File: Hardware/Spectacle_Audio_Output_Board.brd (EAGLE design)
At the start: 25.4 x 55.9 mm, 86 parts, among them J4 AUDIO-JACK3, J5 AUDIO-JACK3, U1 CY8C4146LQI-S422, U2 3.3V, U3 3.3V, U4 AT25SF041-SOIC8, U5 VS1000, Y1 12MHz

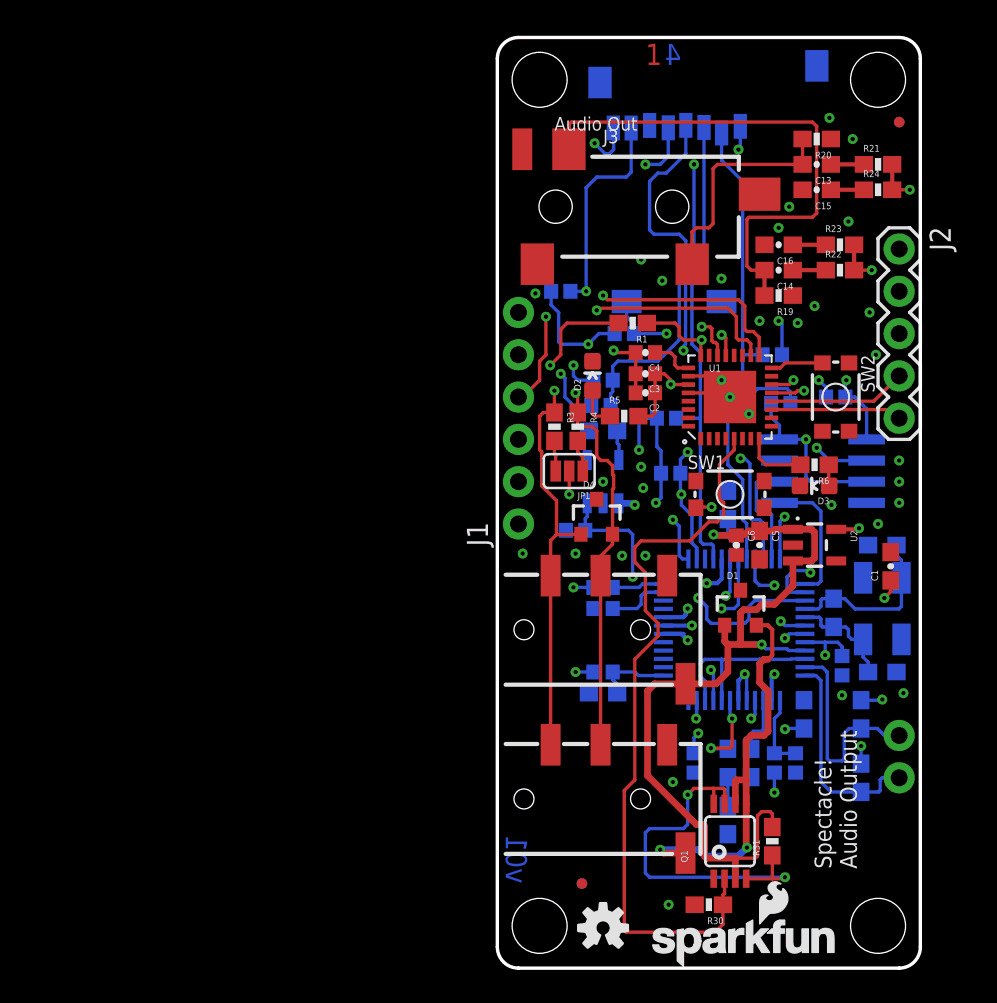
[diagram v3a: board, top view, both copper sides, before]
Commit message: Change pullup resistor values to 4.7k Add firmware to repo
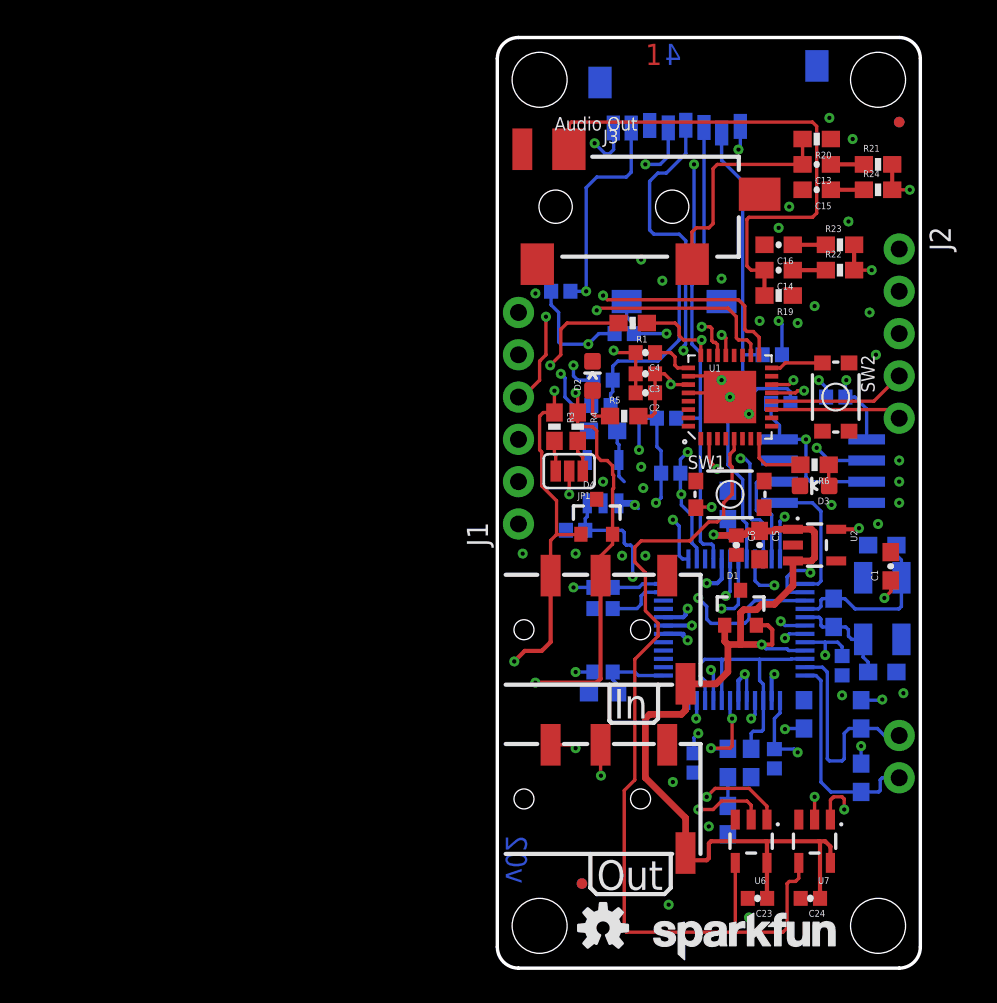
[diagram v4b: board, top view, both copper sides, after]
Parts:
- removed C21: 1.0uF, SparkFun-Capacitors:0402-CAP
- removed Q1: (no value), SparkFun-DiscreteSemi:MSOP8
- removed R30, R31: 10K, SparkFun-Resistors:0603-RES
- added C23, C24: 0.1uF, SparkFun-Capacitors:0402-CAP
- added U6, U7: SN74LVC1G66, SparkFun-AnalogIC:SOT23-5
- J2: device SparkFun-Connectors:1X05 -> SparkFun-Connectors:1X05_NO_SILK
- LOGO2: value SFE_LOGO_NAME_FLAME.1_INCH -> SFE_LOGO_NAME.1_INCH; device SparkFun-Aesthetics:SFE_LOGO_NAME_FLAME_.1 -> SparkFun-Aesthetics:SFE_LOGO_NAME_.1
- R3, R4: value 2.2k -> 4.7K
- moved R26 1.30 mm to (16.6, 12.6)
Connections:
- removed net N$15: C21.1, R26.1, U5.37
- removed net N$26: Q1.4, Q1.7, Q1.8, R31.1
- removed net VOUT: D1.2, J5.EARTH, Q1.5, Q1.6
- removed net V_OUT_EN: Q1.2, R30.1, U1.5
- new net I2C_OUT_EN: U1.5, U6.4, U7.4
- new net POWBTN: R26.1, U1.2, U5.37
- new net SCL_OUT: J5.RING2, U6.2
- new net SDA_OUT: J5.RING1, U7.2
- net 3.3V: no longer C21.2
- net GND: now also C23.2, C24.2, U6.3, U7.3; no longer Q1.1, R30.2
- net SCL: now also U6.1; no longer J5.RING2
- net SDA: now also U7.1; no longer J5.RING1
- net VIN: now also C23.1, C24.1, D1.2, J5.EARTH, U6.5, U7.5; no longer Q1.3, R31.2
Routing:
- net I2C_OUT_EN: track 0.00 -> 54.1 mm
- net V_OUT_EN: track 44.6 -> 0.00 mm
- net SDA: track 40.5 -> 72.9 mm, vias 2 -> 4
- net POWBTN: track 0.00 -> 28.3 mm, vias 0 -> 2
- net VOUT: track 25.1 -> 0.00 mm, vias 2 -> 0
- net N$26: track 23.4 -> 0.00 mm, vias 2 -> 0
- net SCL: track 44.2 -> 65.9 mm, vias 2 -> 4
- net SCL_OUT: track 0.00 -> 19.7 mm, vias 0 -> 2
- net SDA_OUT: track 0.00 -> 17.1 mm, vias 0 -> 2
- net VIN: track 57.1 -> 69.0 mm
- net N$15: track 4.58 -> 0.00 mm
- net VDD: track 26.6 -> 28.0 mm
- net 3.3V: track 31.0 -> 29.8 mm, vias 9 -> 8
- net GND: vias 38 -> 40
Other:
- board text added: "In"
- board text added: "Out"
- board text added: "v02"
- board text removed: "Spectacle\! Audio Output"
- board text removed: "v01"

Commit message: Changes from review/checklist
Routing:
- net VDD: track 28.0 -> 26.6 mm
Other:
- board text added: "Audio Output"
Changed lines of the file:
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@@
 <layers>
 <layer number="1" name="Top" color="4" fill="1" visible="yes" active="yes"/>
-<layer number="2" name="Route2" color="1" fill="3" visible="no" active="yes"/>
-<layer number="15" name="Route15" color="4" fill="6" visible="no" active="yes"/>
+<layer number="2" name="Route2" color="1" fill="3" visible="yes" active="yes"/>
+<layer number="15" name="Route15" color="4" fill="6" visible="yes" active="yes"/>
 <layer number="16" name="Bottom" color="1" fill="1" visible="yes" active="yes"/>
 <layer number="17" name="Pads" color="2" fill="1" visible="yes" active="yes"/>
@@
 <layer number="23" name="tOrigins" color="15" fill="1" visible="yes" active="yes"/>
 <layer number="24" name="bOrigins" color="15" fill="1" visible="yes" active="yes"/>
-<layer number="25" name="tNames" color="7" fill="1" visible="no" active="yes"/>
-<layer number="26" name="bNames" color="7" fill="1" visible="no" active="yes"/>
-<layer number="27" name="tValues" color="7" fill="1" visible="no" active="yes"/>
-<layer number="28" name="bValues" color="7" fill="1" visible="no" active="yes"/>
-<layer number="29" name="tStop" color="7" fill="3" visible="no" active="yes"/>
-<layer number="30" name="bStop" color="7" fill="6" visible="no" active="yes"/>
-<layer number="31" name="tCream" color="7" fill="4" visible="no" active="yes"/>
-<layer number="32" name="bCream" color="7" fill="5" visible="no" active="yes"/>
-<layer number="39" name="tKeepout" color="4" fill="11" visible="no" active="yes"/>
-<layer number="40" name="bKeepout" color="1" fill="11" visible="no" active="yes"/>
-<layer number="41" name="tRestrict" color="4" fill="10" visible="no" active="yes"/>
-<layer number="42" name="bRestrict" color="1" fill="10" visible="no" active="yes"/>
-<layer number="43" name="vRestrict" color="2" fill="10" visible="no" active="yes"/>
-<layer number="44" name="Drills" color="7" fill="1" visible="no" active="yes"/>
+<layer number="25" name="tNames" color="7" fill="1" visible="yes" active="yes"/>
+<layer number="26" name="bNames" color="7" fill="1" visible="yes" active="yes"/>
+<layer number="27" name="tValues" color="7" fill="1" visible="yes" active="yes"/>
+<layer number="28" name="bValues" color="7" fill="1" visible="yes" active="yes"/>
+<layer number="29" name="tStop" color="7" fill="3" visible="yes" active="yes"/>
+<layer number="30" name="bStop" color="7" fill="6" visible="yes" active="yes"/>
+<layer number="31" name="tCream" color="7" fill="4" visible="yes" active="yes"/>
+<layer number="32" name="bCream" color="7" fill="5" visible="yes" active="yes"/>
+<layer number="39" name="tKeepout" color="4" fill="11" visible="yes" active="yes"/>
+<layer number="40" name="bKeepout" color="1" fill="11" visible="yes" active="yes"/>
+<layer number="41" name="tRestrict" color="4" fill="10" visible="yes" active="yes"/>
+<layer number="42" name="bRestrict" color="1" fill="10" visible="yes" active="yes"/>
+<layer number="43" name="vRestrict" color="2" fill="10" visible="yes" active="yes"/>
+<layer number="44" name="Drills" color="7" fill="1" visible="yes" active="yes"/>
 <layer number="45" name="Holes" color="7" fill="1" visible="yes" active="yes"/>
-<layer number="46" name="Milling" color="3" fill="1" visible="no" active="yes"/>
-<layer number="47" name="Measures" color="7" fill="1" visible="no" active="yes"/>
-<layer number="48" name="Document" color="7" fill="1" visible="no" active="yes"/>
-<layer number="49" name="Reference" color="7" fill="1" visible="no" active="yes"/>
+<layer number="46" name="Milling" color="3" fill="1" visible="yes" active="yes"/>
+<layer number="47" name="Measures" color="7" fill="1" visible="yes" active="yes"/>
+<layer number="48" name="Document" color="7" fill="1" visible="yes" active="yes"/>
+<layer number="49" name="Reference" color="7" fill="1" visible="yes" active="yes"/>
 <layer number="51" name="tDocu" color="6" fill="1" visible="yes" active="yes"/>
-<layer number="52" name="bDocu" color="7" fill="1" visible="no" active="yes"/>
+<layer number="52" name="bDocu" color="7" fill="1" visible="yes" active="yes"/>
 <layer number="3" name="Route3" color="4" fill="3" visible="no" active="no"/>
 <layer number="4" name="Route4" color="1" fill="4" visible="no" active="no"/>
@@
 <vertex x="11.281" y="1.541"/>
 </polygon>
-<text x="3.429" y="50.292" size="0.8128" layer="21" font="vector" ratio="15">Audio Out</text>
+<text x="6.858" y="49.022" size="1.27" layer="21" font="vector" ratio="15">Audio Out</text>
 <dimension x1="0" y1="0" x2="0" y2="10.16" x3="-3.81" y3="5.08" textsize="1.27" textratio="15" layer="47" dtype="vertical" unit="inch"/>
 <text x="31.75" y="-13.97" size="1.778" layer="51" font="vector" ratio="15">Mike Hord</text>
@@
 <wire x1="6.858" y1="14.732" x2="6.731" y2="14.859" width="0.254" layer="21"/>
 <wire x1="6.731" y1="14.859" x2="6.731" y2="17.018" width="0.254" layer="21"/>
+<text x="14.986" y="15.113" size="1.27" layer="21" font="vector" ratio="15">Audio
+Output</text>
+<rectangle x1="15.494" y1="34.036" x2="15.621" y2="34.544" layer="41"/>
+<rectangle x1="13.589" y1="35.814" x2="14.351" y2="36.195" layer="41"/>
+<rectangle x1="12.319" y1="33.909" x2="12.573" y2="34.544" layer="41"/>
+<rectangle x1="13.716" y1="32.639" x2="14.224" y2="32.893" layer="41"/>
+<dimension x1="0" y1="0" x2="-3.81" y2="45.72" x3="-12.7" y3="22.86" textsize="1.27" textratio="15" layer="47" dtype="vertical" unit="inch"/>
 </plain>
 <attributes>
@@
 <wire x1="16.24" y1="20.59" x2="16.51" y2="20.32" width="0.254" layer="1"/>
 <wire x1="16.51" y1="20.32" x2="16.51" y2="19.431" width="0.254" layer="1"/>
-<wire x1="8.47" y1="27.598" x2="8.255" y2="27.813" width="0.2032" layer="16"/>
 <wire x1="13.655" y1="19.619" x2="13.655" y2="20.59" width="0.4064" layer="1"/>
 <wire x1="15.875" y1="19.431" x2="16.51" y2="19.431" width="0.254" layer="1"/>
@@
 <wire x1="20.828" y1="10.16" x2="20.701" y2="10.287" width="0.2032" layer="1"/>
 <wire x1="20.701" y1="10.287" x2="20.193" y2="10.287" width="0.2032" layer="1"/>
-<wire x1="20.193" y1="10.287" x2="20.1295" y2="10.2235" width="0.2032" layer="1"/>
-<wire x1="20.1295" y1="10.2235" x2="20.066" y2="10.16" width="0.2032" layer="1"/>
 <wire x1="20" y1="8.9201" x2="20" y2="10.094" width="0.2032" layer="1"/>
-<wire x1="20" y1="10.094" x2="20.066" y2="10.16" width="0.2032" layer="1"/>
+<wire x1="20" y1="10.094" x2="20.193" y2="10.287" width="0.2032" layer="1"/>
 </signal>
 <signal name="N$6">
@@
 <wire x1="9.636575" y1="47.736575" x2="10.144575" y2="47.736575" width="0.2032" layer="16"/>
 <wire x1="10.144575" y1="47.736575" x2="11.318425" y2="48.910425" width="0.2032" layer="16"/>
-<wire x1="7.3" y1="30.5101" x2="7.3" y2="29.53" width="0.2032" layer="16"/>
-<wire x1="7.3" y1="29.53" x2="7.62" y2="29.21" width="0.2032" layer="16"/>
 </signal>
 <signal name="N$1">
@@
 </board>
 </drawing>
+<compatibility>
+<note version="6.3" minversion="6.2.2" severity="warning">
+Since Version 6.2.2 text objects can contain more than one line,
+which will not be processed correctly with this version.
+</note>
+</compatibility>
 </eagle>

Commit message: Fixes from review
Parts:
- moved FRAME1 119.4 mm to (-59.7, 36.8), flipped to the bottom
- moved U$1 78.7 mm to (-39.4, 45.7), flipped to the bottom
- moved FD6 48.3 mm to (-24.1, 50.8), flipped to the top
- moved FD7 48.3 mm to (-24.1, 50.8), flipped to the bottom
- moved J2 48.3 mm to (-24.1, 43.2), flipped to the bottom
- moved J6 48.3 mm to (-24.1, 11.4), flipped to the top
- moved C1 47.2 mm to (-23.6, 24.1), flipped to the bottom
- moved C7 46.2 mm to (-23.1, 25.4), flipped to the top
- moved C8 46.2 mm to (-23.1, 17.8), flipped to the top
- moved Y1 46.2 mm to (-23.1, 21.6), flipped to the top
- moved H1 45.7 mm to (-22.9, 53.3), flipped to the bottom
- moved H3 45.7 mm to (-22.9, 2.54), flipped to the bottom
- moved R21 45.7 mm to (-22.9, 48.3), flipped to the bottom
- moved R24 45.7 mm to (-22.9, 46.7), flipped to the bottom
- moved R27 43.7 mm to (-21.8, 11.4), flipped to the top
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
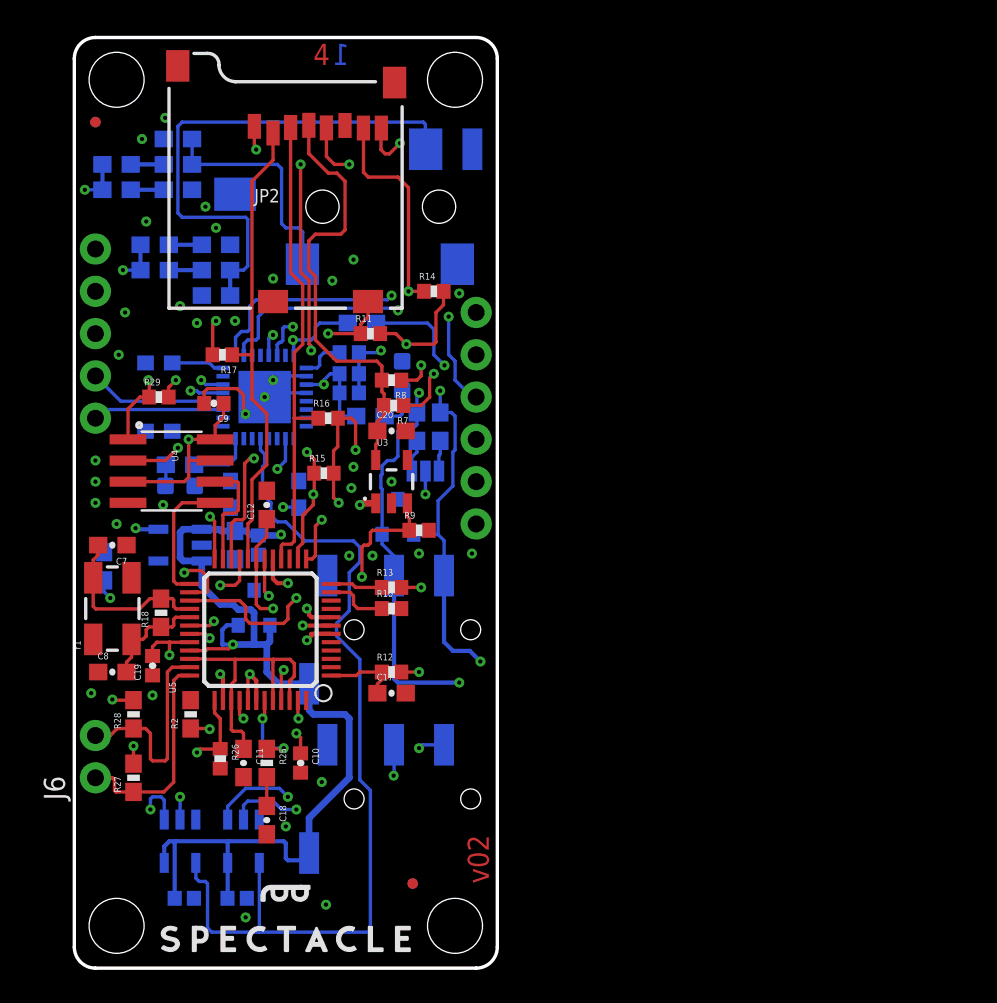
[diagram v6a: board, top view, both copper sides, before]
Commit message: Flipped board to right side up
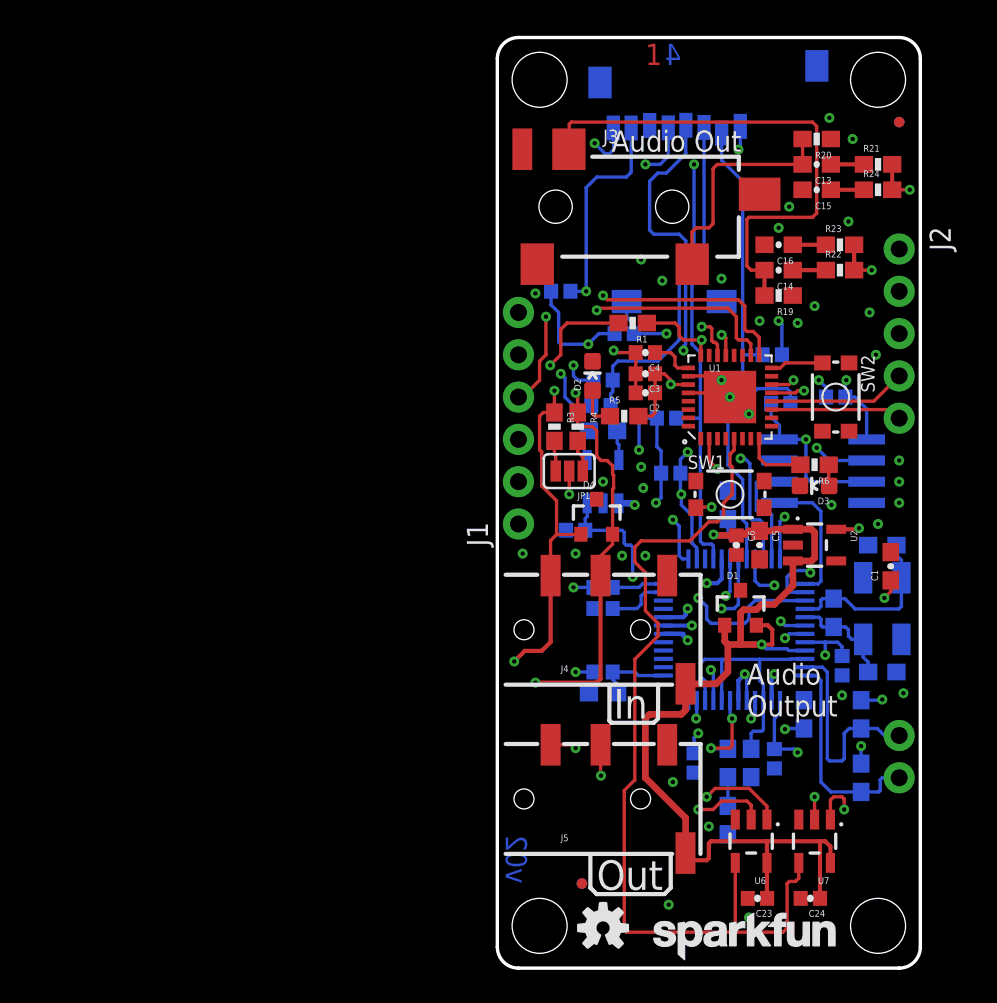
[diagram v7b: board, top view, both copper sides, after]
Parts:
- moved FRAME1 119.4 mm to (59.7, 36.8), flipped to the top
- moved U$1 78.7 mm to (39.4, 45.7), flipped to the top
- moved FD6 48.3 mm to (24.1, 50.8), flipped to the bottom
- moved FD7 48.3 mm to (24.1, 50.8), flipped to the top
- moved J2 48.3 mm to (24.1, 43.2), flipped to the top
- moved J6 48.3 mm to (24.1, 11.4), flipped to the bottom
- moved C1 47.2 mm to (23.6, 24.1), flipped to the top
- moved C7 46.2 mm to (23.1, 25.4), flipped to the bottom
- moved C8 46.2 mm to (23.1, 17.8), flipped to the bottom
- moved Y1 46.2 mm to (23.1, 21.6), flipped to the bottom
- moved H1 45.7 mm to (22.9, 53.3), flipped to the top
- moved H3 45.7 mm to (22.9, 2.54), flipped to the top
- moved R21 45.7 mm to (22.9, 48.3), flipped to the top
- moved R24 45.7 mm to (22.9, 46.7), flipped to the top
- moved R27 43.7 mm to (21.8, 11.4), flipped to the bottom
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
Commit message: Update sch and brd to V10
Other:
- board text added: "v10"
- board text removed: "v02"
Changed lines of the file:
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@@
 <?xml version="1.0" encoding="utf-8"?>
 <!DOCTYPE eagle SYSTEM "eagle.dtd">
-<eagle version="7.6.0">
+<eagle version="7.7.0">
 <drawing>
 <settings>
@@
 <layer number="20" name="Dimension" color="15" fill="1" visible="yes" active="yes"/>
 <layer number="21" name="tPlace" color="16" fill="1" visible="yes" active="yes"/>
-<layer number="22" name="bPlace" color="14" fill="1" visible="no" active="yes"/>
+<layer number="22" name="bPlace" color="14" fill="1" visible="yes" active="yes"/>
 <layer number="23" name="tOrigins" color="15" fill="1" visible="yes" active="yes"/>
-<layer number="24" name="bOrigins" color="15" fill="1" visible="no" active="yes"/>
-<layer number="25" name="tNames" color="7" fill="1" visible="yes" active="yes"/>
+<layer number="24" name="bOrigins" color="15" fill="1" visible="yes" active="yes"/>
+<layer number="25" name="tNames" color="7" fill="1" visible="no" active="yes"/>
 <layer number="26" name="bNames" color="7" fill="1" visible="no" active="yes"/>
 <layer number="27" name="tValues" color="7" fill="1" visible="no" active="yes"/>
@@
 <layer number="43" name="vRestrict" color="2" fill="10" visible="no" active="yes"/>
 <layer number="44" name="Drills" color="7" fill="1" visible="no" active="yes"/>
-<layer number="45" name="Holes" color="7" fill="1" visible="no" active="yes"/>
+<layer number="45" name="Holes" color="7" fill="1" visible="yes" active="yes"/>
 <layer number="46" name="Milling" color="3" fill="1" visible="no" active="yes"/>
 <layer number="47" name="Measures" color="7" fill="1" visible="no" active="yes"/>
 <layer number="48" name="Document" color="7" fill="1" visible="no" active="yes"/>
 <layer number="49" name="Reference" color="7" fill="1" visible="no" active="yes"/>
-<layer number="51" name="tDocu" color="6" fill="1" visible="no" active="yes"/>
+<layer number="51" name="tDocu" color="6" fill="1" visible="yes" active="yes"/>
 <layer number="52" name="bDocu" color="7" fill="1" visible="no" active="yes"/>
 <layer number="3" name="Route3" color="4" fill="3" visible="no" active="no"/>
@@
 <wire x1="24.13" y1="55.88" x2="25.4" y2="54.61" width="0.2032" layer="20" curve="-90"/>
 <text x="90.17" y="36.83" size="1.778" layer="51" font="vector" ratio="15">Mike Hord</text>
-<text x="0.508" y="5.08" size="1.27" layer="16" font="vector" ratio="15" rot="MR90">v02</text>
+<text x="0.508" y="5.08" size="1.27" layer="16" font="vector" ratio="15" rot="MR90">v10</text>
 <text x="8.89" y="54.229" size="1.27" layer="1" font="vector" ratio="15">1</text>
 <text x="8.89" y="52.959" size="1.27" layer="2" font="vector" ratio="15">2</text>
